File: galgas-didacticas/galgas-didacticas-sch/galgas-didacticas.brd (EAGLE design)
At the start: 0 parts

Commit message: Progress
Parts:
- added C1, C2, C5, C6: 100nF, rcl:C0805
- added C3, C4: 22pF, rcl:C0805
- added ICSP: (no value), jumper:JP3Q
- added J1, J2: RJ45_DIRECT, galgas_lib:RJ45_DIRECT
- added JP1: (no value), jumper:JP1
- added Q1: 16MHz, crystal:HC49UP
- added R1: 120, resistor:R0805W
- added U1: ATMEGA328P, atmel:TQFP32-08
- added U2: MAX481CSA, maxim:SO08
- added U3: INA128U, burr-brown:SO08
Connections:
- new net +12V: J1.P3, J2.P3
- new net +5V: U1.4, U1.6
- new net /COMMS_RE: U2.2
- new net COMMS_A: J1.P2, J2.P2, R1.1, U2.6
- new net COMMS_B: J1.P1, J2.P1, JP1.2, U2.7
- new net COMMS_DE: U2.3
- new net COMMS_RX: U2.1
- new net COMMS_TX: U2.4
- new net GND: C1.2, C2.2, C3.1, C4.2, C5.1, C6.1, J1.GND, J1.P4, J2.GND, J2.P4, U1.21, U1.3, U1.5, U2.5
- new net N$1: JP1.1, R1.2
- new net N$2: C6.2, U1.18
- new net N$3: C3.2, Q1.2, U1.7
- new net N$4: C4.1, Q1.1, U1.8
- new net N$5: C5.2, U1.20
- new net V+: U3.7
- new net V-: U3.4
- new net VCC: C1.1, C2.1, U2.8
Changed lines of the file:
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@@
 <layer number="51" name="tDocu" color="7" fill="1" visible="yes" active="yes"/>
 <layer number="52" name="bDocu" color="7" fill="1" visible="yes" active="yes"/>
+<layer number="90" name="Modules" color="5" fill="1" visible="no" active="no"/>
+<layer number="91" name="Nets" color="2" fill="1" visible="no" active="no"/>
+<layer number="92" name="Busses" color="1" fill="1" visible="no" active="no"/>
+<layer number="93" name="Pins" color="2" fill="1" visible="no" active="no"/>
+<layer number="94" name="Symbols" color="4" fill="1" visible="no" active="no"/>
+<layer number="95" name="Names" color="7" fill="1" visible="no" active="no"/>
+<layer number="96" name="Values" color="7" fill="1" visible="no" active="no"/>
+<layer number="97" name="Info" color="7" fill="1" visible="no" active="no"/>
+<layer number="98" name="Guide" color="6" fill="1" visible="no" active="no"/>
+<layer number="99" name="SpiceOrder" color="5" fill="1" visible="no" active="no"/>
 </layers>
 <board>
@@
 </autorouter>
 <elements>
+<element name="J1" library="galgas_lib" package="RJ45_DIRECT" value="RJ45_DIRECT" x="41.91" y="6.35"/>
+<element name="J2" library="galgas_lib" package="RJ45_DIRECT" value="RJ45_DIRECT" x="41.91" y="26.67"/>
+<element name="U2" library="maxim" package="SO08" value="MAX481CSA" x="15.24" y="20.32">
+<attribute name="OC_NEWARK" value="90C3817" x="15.24" y="20.32" size="1.778" layer="27" display="off"/>
+<attribute name="OC_FARNELL" value="unknown" x="15.24" y="20.32" size="1.778" layer="27" display="off"/>
+<attribute name="MPN" value="MAX481CSA" x="15.24" y="20.32" size="1.778" layer="27" display="off"/>
+<attribute name="MF" value="MAXIM" x="15.24" y="20.32" size="1.778" layer="27" display="off"/>
+</element>
+<element name="R1" library="resistor" package="R0805W" value="120" x="17.78" y="5.08" rot="R180"/>
+<element name="JP1" library="jumper" package="JP1" value="" x="7.62" y="7.62"/>
+<element name="C1" library="rcl" package="C0805" value="100nF" x="7.62" y="21.59" rot="R270"/>
+<element name="U3" library="burr-brown" package="SO08" value="INA128U" x="8.89" y="-7.62">
+<attribute name="OC_NEWARK" value="35C1729" x="8.89" y="-7.62" size="1.778" layer="27" display="off"/>
+<attribute name="OC_FARNELL" value="1212413" x="8.89" y="-7.62" size="1.778" layer="27" display="off"/>
+<attribute name="MPN" value="INA128U" x="8.89" y="-7.62" size="1.778" layer="27" display="off"/>
+<attribute name="MF" value="TEXAS INSTRUMENTS" x="8.89" y="-7.62" size="1.778" layer="27" display="off"/>
+</element>
+<element name="U1" library="atmel" package="TQFP32-08" value="ATMEGA328P" x="-1.27" y="-6.35">
+<attribute name="OC_NEWARK" value="73M8863" x="-1.27" y="-6.35" size="1.778" layer="27" display="off"/>
+<attribute name="OC_FARNELL" value="9171371" x="-1.27" y="-6.35" size="1.778" layer="27" display="off"/>
+<attribute name="MPN" value="ATMEGA8-16AU" x="-1.27" y="-6.35" size="1.778" layer="27" display="off"/>
+<attribute name="MF" value="" x="-1.27" y="-6.35" size="1.778" layer="27" display="off"/>
+</element>
+<element name="Q1" library="crystal" package="HC49UP" value="16MHz" x="2.54" y="-16.51">
+<attribute name="OC_NEWARK" value="unknown" x="2.54" y="-16.51" size="1.778" layer="27" display="off"/>
+<attribute name="OC_FARNELL" value="unknown" x="2.54" y="-16.51" size="1.778" layer="27" display="off"/>
+<attribute name="MPN" value="" x="2.54" y="-16.51" size="1.778" layer="27" display="off"/>
+<attribute name="MF" value="" x="2.54" y="-16.51" size="1.778" layer="27" display="off"/>
+</element>
+<element name="C2" library="rcl" package="C0805" value="100nF" x="-3.81" y="-25.4"/>
+<element name="C3" library="rcl" package="C0805" value="22pF" x="-3.81" y="-31.75"/>
+<element name="C4" library="rcl" package="C0805" value="22pF" x="-3.81" y="-38.1"/>
+<element name="C5" library="rcl" package="C0805" value="100nF" x="-3.81" y="-44.45"/>
+<element name="C6" library="rcl" package="C0805" value="100nF" x="-3.81" y="-50.8"/>
+<element name="ICSP" library="jumper" package="JP3Q" value="" x="-11.43" y="-46.99"/>
 </elements>
 <signals>
+<signal name="GND">
+<contactref element="J1" pad="GND"/>
+<contactref element="J2" pad="GND"/>
+<contactref element="J1" pad="P4"/>
+<contactref element="J2" pad="P4"/>
+<contactref element="U2" pad="5"/>
+<contactref element="C1" pad="2"/>
+<contactref element="U1" pad="3"/>
+<contactref element="U1" pad="5"/>
+<contactref element="U1" pad="21"/>
+<contactref element="C2" pad="2"/>
+<contactref element="C3" pad="1"/>
+<contactref element="C4" pad="2"/>
+<contactref element="C5" pad="1"/>
+<contactref element="C6" pad="1"/>
+<wire x1="32.91" y1="27.305" x2="49.91" y2="26.67" width="0" layer="19" extent="1-1"/>
+<wire x1="17.145" y1="23.3934" x2="32.91" y2="27.305" width="0" layer="19" extent="1-1"/>
+<wire x1="7.62" y1="20.64" x2="17.145" y2="23.3934" width="0" layer="19" extent="1-1"/>
+<wire x1="49.91" y1="6.35" x2="49.91" y2="26.67" width="0" layer="19" extent="1-1"/>
+<wire x1="32.91" y1="6.985" x2="49.91" y2="6.35" width="0" layer="19" extent="1-1"/>
+<wire x1="3.0226" y1="-5.95" x2="7.62" y2="20.64" width="0" layer="19" extent="1-1"/>
+<wire x1="-5.5626" y1="-5.15" x2="3.0226" y2="-5.95" width="0" layer="19" extent="1-1"/>
+<wire x1="-5.5626" y1="-6.75" x2="-5.5626" y2="-5.15" width="0" layer="19" extent="1-1"/>
+<wire x1="-2.86" y1="-25.4" x2="-5.5626" y2="-6.75" width="0" layer="19" extent="1-1"/>
+<wire x1="-4.76" y1="-31.75" x2="-2.86" y2="-25.4" width="0" layer="19" extent="1-1"/>
+<wire x1="-2.86" y1="-38.1" x2="-4.76" y2="-31.75" width="0" layer="19" extent="1-1"/>
+<wire x1="-4.76" y1="-44.45" x2="-2.86" y2="-38.1" width="0" layer="19" extent="1-1"/>
+<wire x1="-4.76" y1="-50.8" x2="-4.76" y2="-44.45" width="0" layer="19" extent="1-1"/>
+</signal>
+<signal name="COMMS_B">
+<contactref element="J1" pad="P1"/>
+<contactref element="J2" pad="P1"/>
+<contactref element="U2" pad="7"/>
+<contactref element="JP1" pad="2"/>
+<wire x1="14.605" y1="23.3934" x2="32.91" y2="31.115" width="0" layer="19" extent="1-1"/>
+<wire x1="32.91" y1="10.795" x2="32.91" y2="31.115" width="0" layer="19" extent="1-1"/>
+<wire x1="7.62" y1="8.89" x2="32.91" y2="10.795" width="0" layer="19" extent="1-1"/>
+</signal>
+<signal name="COMMS_A">
+<contactref element="J1" pad="P2"/>
+<contactref element="J2" pad="P2"/>
+<contactref element="U2" pad="6"/>
+<contactref element="R1" pad="1"/>
+<wire x1="15.875" y1="23.3934" x2="32.91" y2="29.845" width="0" layer="19" extent="1-1"/>
+<wire x1="32.91" y1="9.525" x2="32.91" y2="29.845" width="0" layer="19" extent="1-1"/>
+<wire x1="18.8325" y1="5.08" x2="32.91" y2="9.525" width="0" layer="19" extent="1-1"/>
+</signal>
+<signal name="+12V">
+<contactref element="J1" pad="P3"/>
+<contactref element="J2" pad="P3"/>
+<wire x1="32.91" y1="28.575" x2="32.91" y2="8.255" width="0" layer="19" extent="1-1"/>
+</signal>
+<signal name="VCC">
+<contactref element="U2" pad="8"/>
+<contactref element="C1" pad="1"/>
+<contactref element="C2" pad="1"/>
+<wire x1="7.62" y1="22.54" x2="13.335" y2="23.3934" width="0" layer="19" extent="1-1"/>
+<wire x1="-4.76" y1="-25.4" x2="7.62" y2="22.54" width="0" layer="19" extent="1-1"/>
+</signal>
+<signal name="COMMS_TX">
+<contactref element="U2" pad="4"/>
+</signal>
+<signal name="COMMS_DE">
+<contactref element="U2" pad="3"/>
+</signal>
+<signal name="/COMMS_RE">
+<contactref element="U2" pad="2"/>
+</signal>
+<signal name="COMMS_RX">
+<contactref element="U2" pad="1"/>
+</signal>
+<signal name="N$1">
+<contactref element="R1" pad="2"/>
+<contactref element="JP1" pad="1"/>
+<wire x1="16.7275" y1="5.08" x2="7.62" y2="6.35" width="0" layer="19" extent="1-1"/>
+</signal>
+<signal name="V+">
+<contactref element="U3" pad="7"/>
+</signal>
+<signal name="V-">
+<contactref element="U3" pad="4"/>
+</signal>
+<signal name="+5V">
+<contactref element="U1" pad="4"/>
+<contactref element="U1" pad="6"/>
+<wire x1="-5.5626" y1="-7.55" x2="-5.5626" y2="-5.95" width="0" layer="19" extent="1-1"/>
+</signal>
+<signal name="N$3">
+<contactref element="U1" pad="7"/>
+<contactref element="C3" pad="2"/>
+<contactref element="Q1" pad="2"/>
+<wire x1="7.366" y1="-16.51" x2="-2.86" y2="-31.75" width="0" layer="19" extent="1-1"/>
+<wire x1="-5.5626" y1="-8.35" x2="7.366" y2="-16.51" width="0" layer="19" extent="1-1"/>
+</signal>
+<signal name="N$4">
+<contactref element="U1" pad="8"/>
+<contactref element="C4" pad="1"/>
+<contactref element="Q1" pad="1"/>
+<wire x1="-2.286" y1="-16.51" x2="-4.76" y2="-38.1" width="0" layer="19" extent="1-1"/>
+<wire x1="-5.5626" y1="-9.15" x2="-2.286" y2="-16.51" width="0" layer="19" extent="1-1"/>
+</signal>
+<signal name="N$5">
+<contactref element="U1" pad="20"/>
+<contactref element="C5" pad="2"/>
+<wire x1="3.0226" y1="-6.75" x2="-2.86" y2="-44.45" width="0" layer="19" extent="1-1"/>
+</signal>
+<signal name="N$2">
+<contactref element="U1" pad="18"/>
+<contactref element="C6" pad="2"/>
+<wire x1="3.0226" y1="-8.35" x2="-2.86" y2="-50.8" width="0" layer="19" extent="1-1"/>
+</signal>
 </signals>
 </board>

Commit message: progress
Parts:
- added C10: 1uF, rcl:C0805
- added C11, C8, C9: 100nF, rcl:C0805
- added C12: 10uF, rcl:C0805
- added C13, C14: 10uF, rcl:153CLV-0505
- added C7: 4.7uF/50V C1206C475K5PACTU, rcl:C1206K
- added JP3: (no value), jumper:JP2
- added L1: 6.8uF MLZ2012N6R8LT000, rcl:R0805W
- added R2: 100, rcl:R0805W
- added R3, R4, R5: 350, resistor:R1206W
- added U$1: PEM1-S12-D5-S, galgas_lib:PEM1-S
- added U$2: REF3325, galgas_lib:SOT-23
- added U$3: MCP3421, galgas_lib:SOT-23-6
- moved C5 110.7 mm to (62.2, 44.5)
- moved ICSP 100.0 mm to (34.3, 41.9)
- moved C4 98.5 mm to (45.7, 47.0)
- moved C6 94.4 mm to (27.9, 38.1)
- moved C2 82.7 mm to (11.4, 55.9)
- moved C3 76.7 mm to (21.6, 40.6)
- moved U3 65.4 mm to (35.6, 52.1)
- moved Q1 42.2 mm to (7.62, 25.4), turned to 90 degrees
- moved JP1 39.2 mm to (43.2, 24.1)
- moved U1 38.8 mm to (19.1, 26.7)
- moved U2 33.0 mm to (24.1, 52.1), turned to 270 degrees
- moved R1 29.0 mm to (43.2, 19.1), turned to 90 degrees
- moved C1 23.3 mm to (16.5, 43.2)
- moved J1 17.0 mm to (57.1, 14.0)
- moved J2 16.5 mm to (57.1, 33.0)
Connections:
- removed net V+: U3.7
- removed net V-: U3.4
- new net -5V: C14.-, C8.1, U$1.5, U3.4
- new net /RESET: ICSP.3
- new net AGND: C7.2, J1.P4, J2.P4, U$1.2
- new net G1: U$3.1, U3.6
- new net G1N: R3.1, R4.2, U3.2
- new net G1P: JP3.2, U3.3
- new net MISO: ICSP.1
- new net MOSI: ICSP.5
- new net N$15: JP3.3, R5.2
- new net N$6: L1.2, U$1.1
- new net N$7: R2.1, U3.1
- new net N$8: R2.2, U3.8
- new net SCK: ICSP.2
- new net SCL: U$3.3
- new net SDA: U$3.4
- new net VREF_2.5V: C10.1, U$2.2, U$3.6, U3.5
- net +12V: now also C7.1, L1.1
- net +5V: now also C11.2, C12.2, C13.+, C9.1, ICSP.6, JP3.1, R3.2, U$1.7, U$2.1, U$3.5, U3.7
- net GND: now also C10.2, C11.1, C12.1, C13.-, C14.+, C8.2, C9.2, ICSP.4, R4.1, R5.1, U$1.6, U$2.3, U$3.2; no longer J1.P4, J2.P4
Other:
- board outline added: 70 x 60 mm

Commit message: First "final" version of the SCH
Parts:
- removed U$1: PEM1-S12-D5-S, galgas_lib:PEM1-S
- removed U$3: MCP3421, galgas_lib:SOT-23-6
- added LED1, LED2: (no value), jumper:JP1
- added PT1: 2PT_GND_TIE, SparkFun-Passives:2PT_GND_TIE
- added PWR1: PEM1-S12-D5-S, galgas_lib:PEM1-S
- added Q2, Q3: 2N7002PW, SparkFun-DiscreteSemi:SOT323
- added R6: 10K, resistor:R0805W
- added S1: (no value), SparkFun-Electromechanical:TACTILE-PTH
- added U4: MCP3421, galgas_lib:SOT-23-6
- added U5: REF3325, galgas_lib:SOT-23
- U$2: value REF3325 -> SUPPLY_CONNECT; device galgas_lib:SOT-23 -> SparkFun-Passives:2PT_GND_TIE
- moved C14 100.6 mm to (38.1, 14.0)
- moved JP3 97.7 mm to (7.62, 38.1)
- moved R4 94.9 mm to (35.6, 29.2)
- moved R5 88.0 mm to (33.0, 17.8)
- moved C13 85.7 mm to (31.8, 7.62)
- moved R3 84.1 mm to (29.2, 25.4)
- moved ICSP 75.8 mm to (-14.0, -16.5)
- moved C12 68.3 mm to (24.1, 20.3)
- moved C11 54.8 mm to (15.2, 15.2)
- moved U$2 50.8 mm to (-47.0, -21.6)
- moved C10 37.7 mm to (22.9, 5.08)
- moved C9 28.5 mm to (17.8, 7.62)
- moved C8 22.7 mm to (12.7, 10.2)
- moved R2 11.7 mm to (5.08, 7.62)
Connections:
- new net LED1_PWM: Q2.1, U1.13
- new net LED2_PWM: Q3.1, U1.14
- new net N$9: LED2.1, Q3.3
- net +12V: now also LED1.2, LED2.2
- net +5V: now also C6.2, ICSP.2, PWR1.7, R6.1, U$2.P$1, U1.18, U4.5, U5.1; no longer ICSP.6, U$1.7, U$2.1, U$3.5
- net -5V: now also PWR1.5; no longer U$1.5
- net /COMMS_RE: now also U1.1
- net /RESET: now also ICSP.5, R6.2, S1.3, U1.29; no longer ICSP.3
- net AGND: now also PT1.P$1, PWR1.2, Q2.2, Q3.2; no longer U$1.2
- net COMMS_DE: now also U1.32
- net COMMS_RX: now also U1.30
- net COMMS_TX: now also U1.31
- net G1: now also U4.1; no longer U$3.1
- net GND: now also ICSP.6, PT1.P$2, PWR1.6, S1.1, U4.2, U5.3; no longer ICSP.4, U$1.6, U$2.3, U$3.2
- net MISO: now also U1.16
- net MOSI: now also ICSP.4, U1.15; no longer ICSP.5
- net N$2: now also LED1.1, Q2.3; no longer C6.2, U1.18
- net N$6: now also PWR1.1; no longer U$1.1
- net SCK: now also ICSP.3, U1.17; no longer ICSP.2
- net SCL: now also U1.28, U4.3; no longer U$3.3
- net SDA: now also U1.27, U4.4; no longer U$3.4
- net VCC: now also U$2.P$2
- net VREF_2.5V: now also U4.6, U5.2; no longer U$2.2, U$3.6

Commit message: Board routing done
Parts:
- Q1: value 16MHz -> 16M
- moved PT1 93.5 mm to (43.2, 17.1), turned to 180 degrees
- moved LED2 84.9 mm to (34.3, 27.3), turned to 270 degrees
- moved U$2 84.5 mm to (10.8, 40.0), turned to 270 degrees
- moved LED1 81.3 mm to (34.3, 31.8), turned to 270 degrees
- moved Q2 72.8 mm to (29.2, 31.8), turned to 270 degrees
- moved Q3 72.4 mm to (29.2, 27.3), turned to 270 degrees
- moved U5 67.1 mm to (35.6, 39.4), turned to 180 degrees
- moved U4 64.8 mm to (30.5, 44.5), turned to 270 degrees
- moved JP3 53.3 mm to (59.7, 49.5), turned to 270 degrees
- moved R2 53.0 mm to (37.5, 49.5), turned to 90 degrees
- moved C9 52.6 mm to (40.0, 55.2), turned to 180 degrees
- moved PWR1 50.6 mm to (38.1, 5.08), turned to 90 degrees
- moved C4 50.2 mm to (6.35, 15.9)
- moved C5 48.6 mm to (21.6, 17.8), turned to 90 degrees
- moved C8 44.5 mm to (43.8, 41.9), turned to 270 degrees
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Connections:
- net +12V: now also J1.P8, J2.P8; no longer J1.P3, J2.P3
- net +5V: now also C2.1
- net AGND: now also J1.P6, J2.P6; no longer J1.P4, J2.P4
- net VCC: no longer C2.1
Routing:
- net GND: track 0.00 -> 278.5 mm, vias 0 -> 3
- net +5V: track 0.00 -> 229.6 mm, vias 0 -> 5
- net AGND: track 0.00 -> 93.6 mm
- net COMMS_B: track 0.00 -> 62.8 mm, vias 0 -> 1
- net COMMS_A: track 0.00 -> 56.8 mm, vias 0 -> 2
- net +12V: track 0.00 -> 52.0 mm, vias 0 -> 1
- net -5V: track 0.00 -> 44.1 mm
- net LED2_PWM: track 0.00 -> 43.2 mm
- net VREF_2.5V: track 0.00 -> 33.7 mm
- net /RESET: track 0.00 -> 31.2 mm, vias 0 -> 1
- net G1: track 0.00 -> 24.6 mm
- net G1P: track 0.00 -> 22.8 mm
- net LED1_PWM: track 0.00 -> 21.6 mm
- net SDA: track 0.00 -> 21.3 mm
- net SCL: track 0.00 -> 20.3 mm
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- added copper zone on layer 1, net GND
- added copper zone on layer 16, net GND
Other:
- board text added: "+"
- board text added: "Galgas-2-LED"
- board text added: "Universidad de Almería (C) 2019"

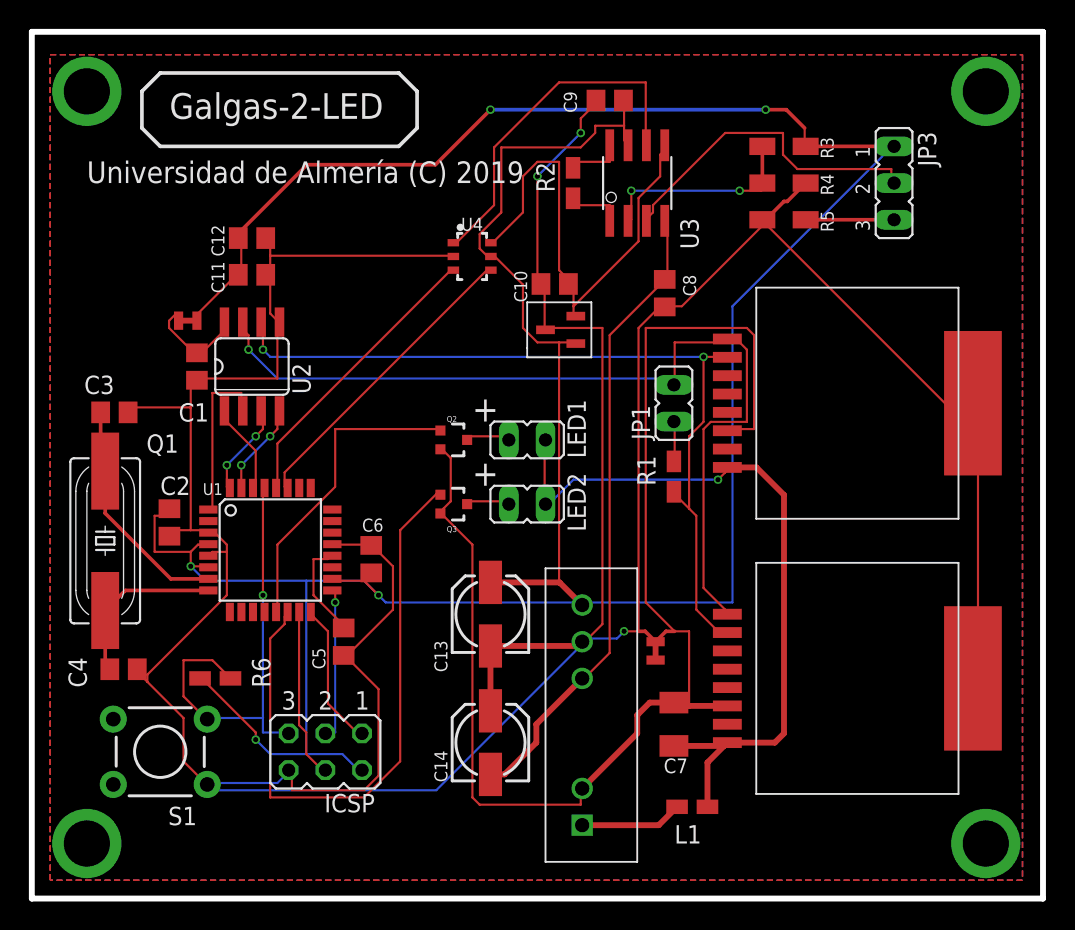
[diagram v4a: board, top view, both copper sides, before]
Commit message: mejoras (más condensadores desacoplo, etc.)
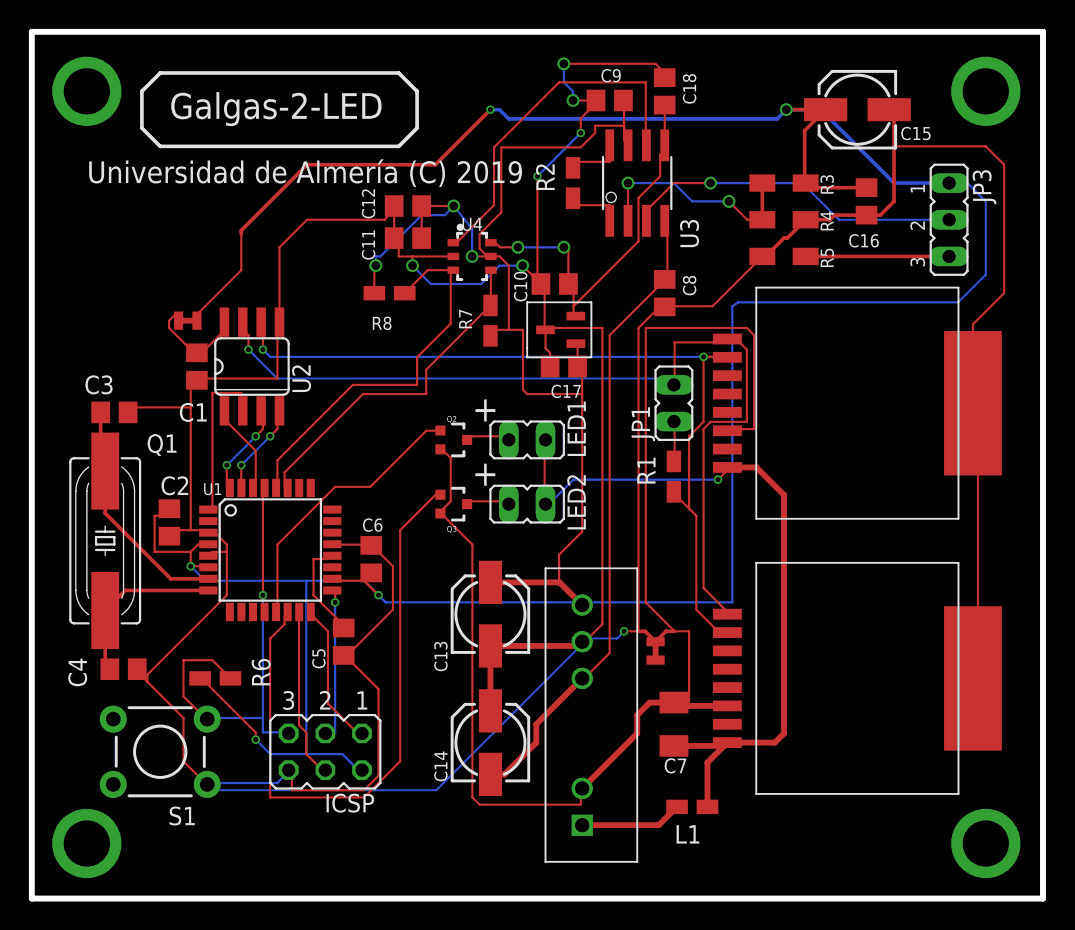
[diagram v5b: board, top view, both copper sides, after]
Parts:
- added C15: 100uF, rcl:153CLV-0505
- added C16, C17, C18: 100nF, rcl:C0805
- added R7, R8: 3.3K, resistor:R0805W
- moved C11 11.1 mm to (26.0, 45.7), turned to 0 degrees
- moved C12 11.0 mm to (26.0, 47.9), turned to 0 degrees
- moved JP3 4.58 mm to (63.5, 47.0)
- moved R3 2.54 mm to (52.1, 49.5)
- moved R4 2.54 mm to (52.1, 47.0)
- moved R5 2.54 mm to (52.1, 44.5)
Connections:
- net +5V: now also C15.+, C16.1, C17.1, R7.1, R8.1
- net GND: now also C15.-, C16.2, C17.2, C18.1
- net SCL: now also R8.2
- net SDA: now also R7.2
- net VREF_2.5V: now also C18.2
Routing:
- net +5V: track 229.6 -> 284.6 mm, vias 5 -> 8
- net GND: track 278.5 -> 324.2 mm, vias 3 -> 7
- net SCL: track 20.3 -> 26.7 mm
- net VREF_2.5V: track 33.7 -> 27.7 mm, vias 0 -> 2
- net N$15: track 6.12 -> 9.93 mm
- net SDA: track 21.3 -> 24.0 mm
- net LED1_PWM: track 21.6 -> 19.5 mm
- net G1N: track 14.4 -> 15.5 mm
- net G1P: track 22.8 -> 23.5 mm, vias 0 -> 1
- removed copper zone on layer 1, net GND
- removed copper zone on layer 16, net GND
